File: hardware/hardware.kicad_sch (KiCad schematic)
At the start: 73 parts, among them J1 USB_B, J2 AUDIO, J3 STYLUS, SW1 SW_POWER, U1 NE555P, U2 LM386, U3 LM3914V

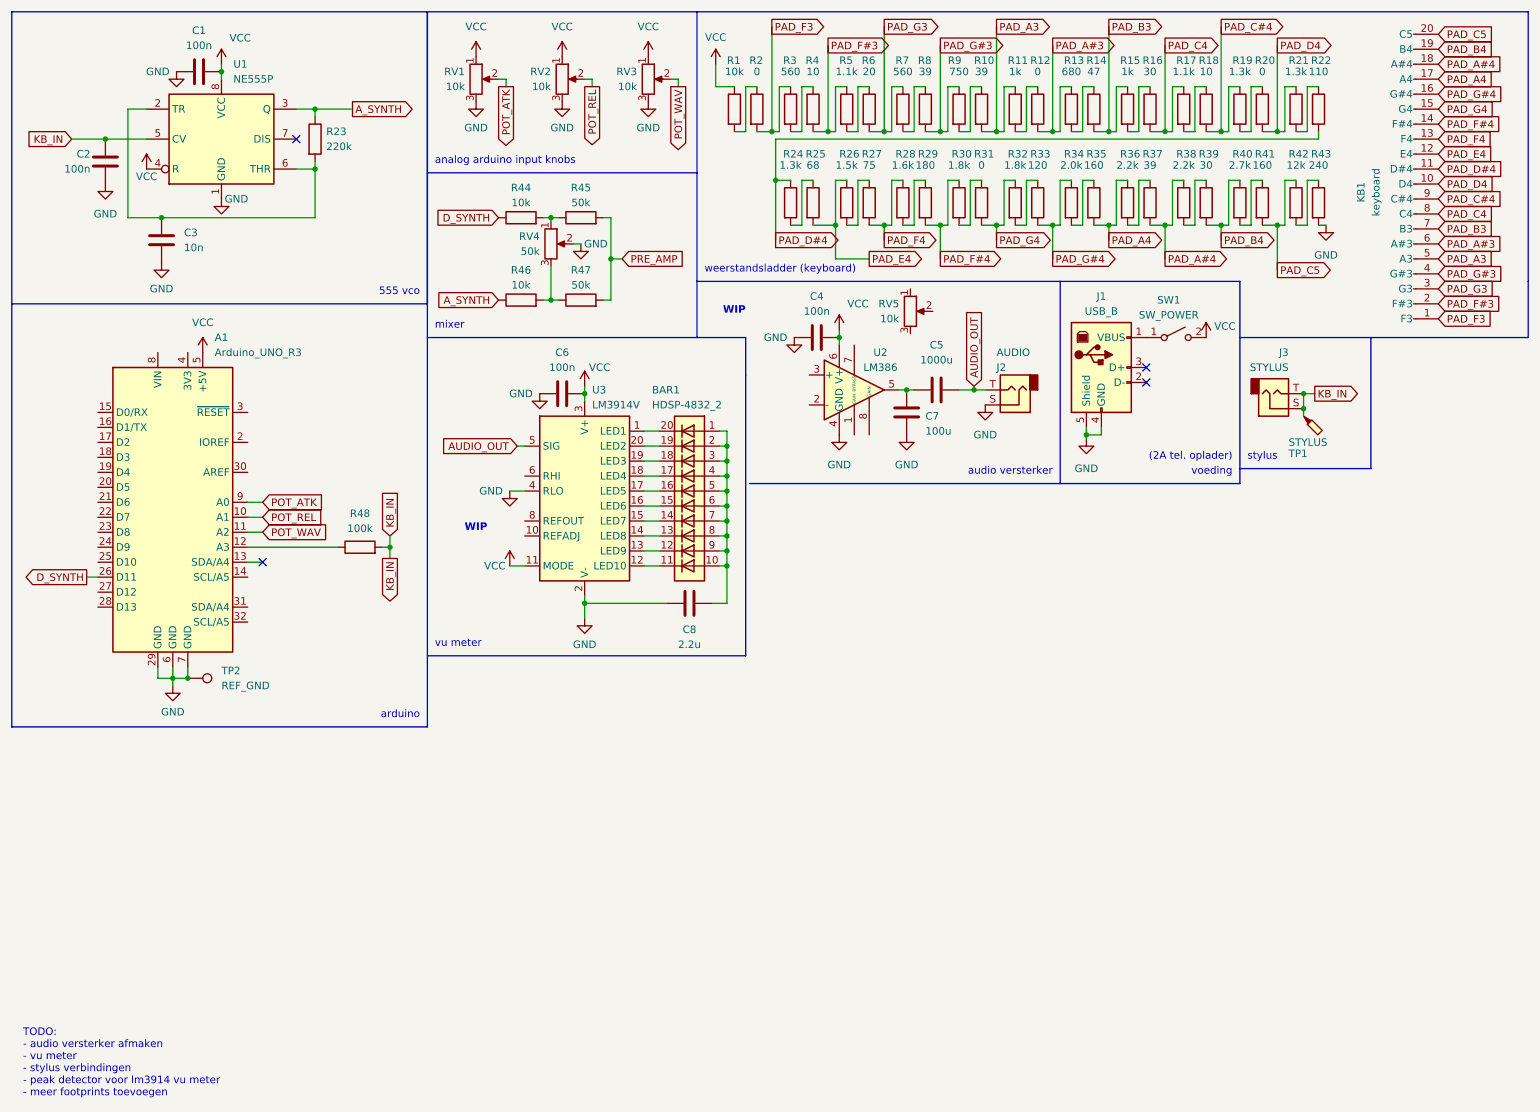
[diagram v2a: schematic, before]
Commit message: more hardware
amplifier circuit done
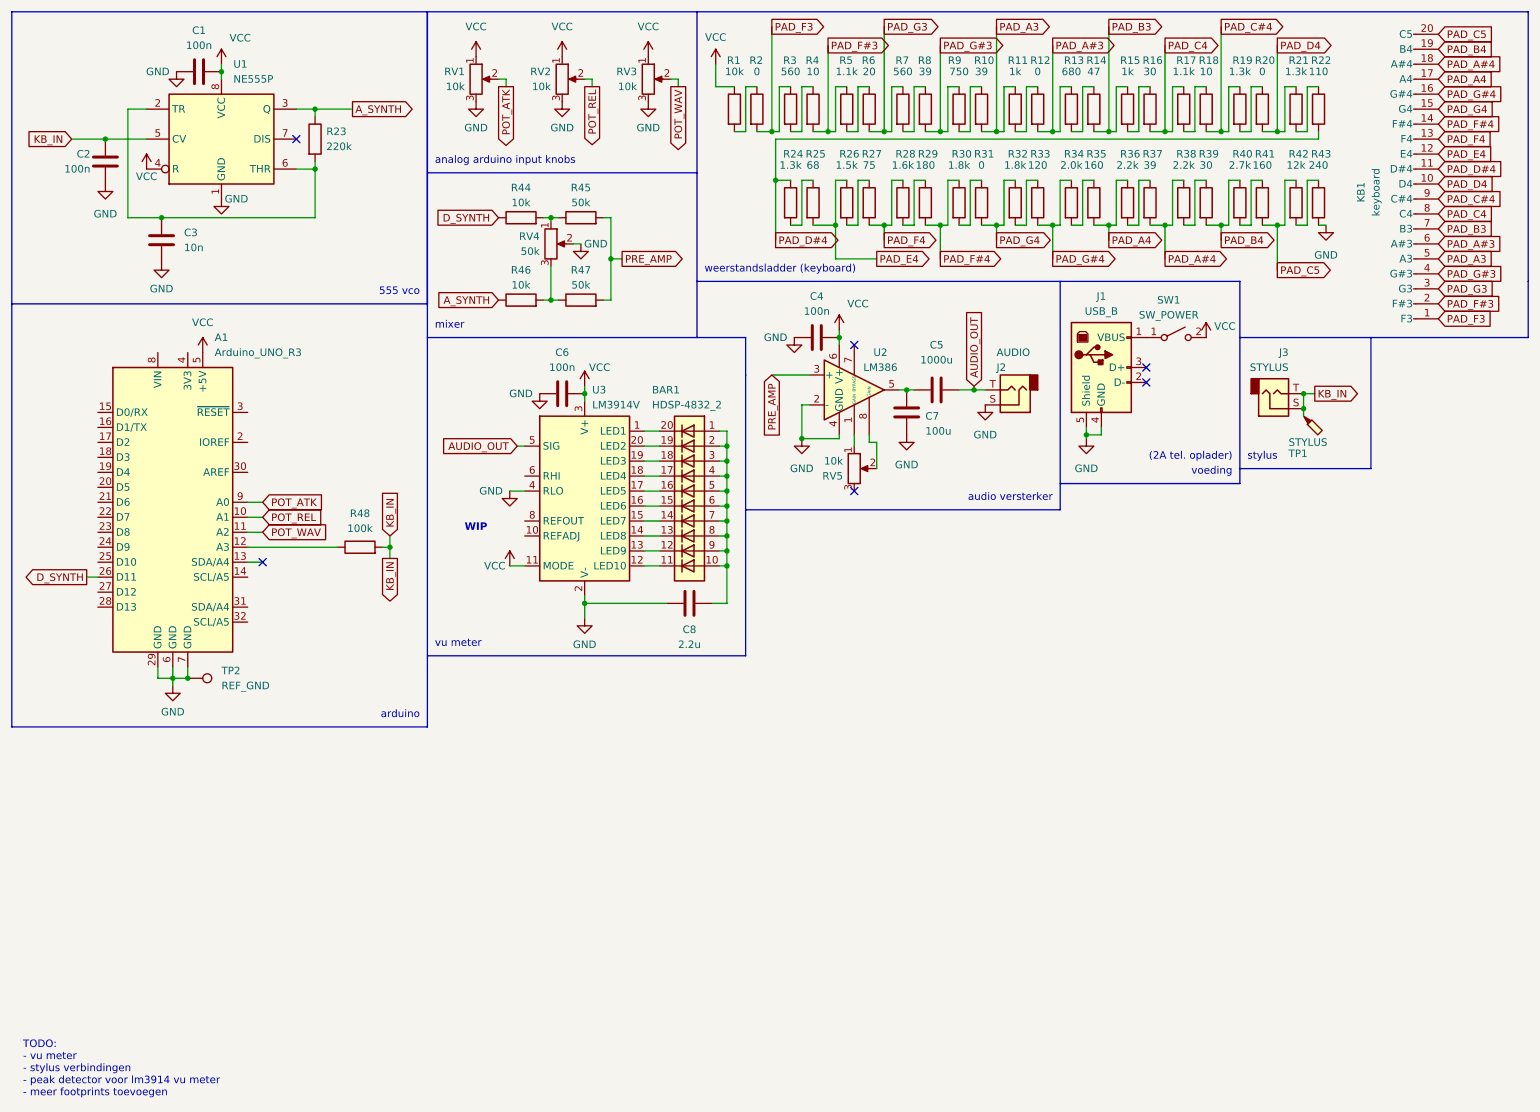
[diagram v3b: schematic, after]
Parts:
- U2: footprint (none) -> Package_DIP:DIP-8_W7.62mm
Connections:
- net GND: now also U2.2 (-)
- net PRE_AMP: now also U2.3 (+)
- net at RV5.1: now also U2.1 (GAIN)
- net at RV5.2: now also U2.8 (GAIN)
- no-connect marks 4 -> 6
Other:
- note added: "TODO: - vu meter - stylus verbindingen - peak detector voor lm3914 vu meter - meer footprints toevoegen"
- note removed: "TODO: - audio versterker afmaken - vu meter - stylus verbindingen - peak detector voor lm3914 vu meter - meer footprints toevoegen"
- moved on the sheet: RV5
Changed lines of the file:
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@@
   (junction (at 198.12 48.26) (diameter 0) (color 0 0 0 0)
   )
+  (junction (at 146.05 84.455) (diameter 0) (color 0 0 0 0)
+  )
   (junction (at 179.07 48.26) (diameter 0) (color 0 0 0 0)
   )
+  (no_connect (at 154.94 68.58))
   (no_connect (at 204.47 74.93))
+  (no_connect (at 154.94 93.345))
   (no_connect (at 54.61 105.41))
   (no_connect (at 204.47 72.39))
@@
     (stroke (width 0) (type default) (color 0 0 0 0))
   )
-  (wire (pts (xy 151.765 53.975) (xy 157.48 53.975))
-    (stroke (width 0) (type default) (color 0 0 0 0))
-  )
   (polyline (pts (xy 128.27 12.065) (xy 128.27 39.37))
     (stroke (width 0) (type default) (color 0 0 0 0))
@@
     (stroke (width 0) (type default) (color 0 0 0 0))
   )
-  (polyline (pts (xy 137.16 92.075) (xy 189.865 92.075))
+  (polyline (pts (xy 136.525 96.52) (xy 189.865 96.52))
     (stroke (width 0) (type default) (color 0 0 0 0))
   )
@@
     (stroke (width 0) (type default) (color 0 0 0 0))
   )
-  (polyline (pts (xy 189.865 92.075) (xy 189.865 57.785))
+  (polyline (pts (xy 189.865 96.52) (xy 189.865 57.785))
     (stroke (width 0) (type default) (color 0 0 0 0))
   )
@@
     (stroke (width 0) (type default) (color 0 0 0 0))
   )
+  (polyline (pts (xy 189.865 92.075) (xy 220.345 92.075))
+    (stroke (width 0) (type default) (color 0 0 0 0))
+  )
   (wire (pts (xy 217.17 48.26) (xy 217.17 50.8))
     (stroke (width 0) (type default) (color 0 0 0 0))
@@
     (stroke (width 0) (type default) (color 0 0 0 0))
   )
+  (wire (pts (xy 147.32 78.74) (xy 146.05 78.74))
+    (stroke (width 0) (type default) (color 0 0 0 0))
+  )
   (wire (pts (xy 133.35 83.185) (xy 132.08 83.185))
     (stroke (width 0) (type default) (color 0 0 0 0))
@@
     (stroke (width 0) (type default) (color 0 0 0 0))
   )
+  (wire (pts (xy 146.05 78.74) (xy 146.05 84.455))
+    (stroke (width 0) (type default) (color 0 0 0 0))
+  )
   (wire (pts (xy 121.92 100.965) (xy 119.38 100.965))
     (stroke (width 0) (type default) (color 0 0 0 0))
@@
     (stroke (width 0) (type default) (color 0 0 0 0))
   )
+  (wire (pts (xy 140.97 73.66) (xy 147.32 73.66))
+    (stroke (width 0) (type default) (color 0 0 0 0))
+  )
   (wire (pts (xy 167.005 48.26) (xy 169.545 48.26))
     (stroke (width 0) (type default) (color 0 0 0 0))
@@
     (stroke (width 0) (type default) (color 0 0 0 0))
   )
+  (wire (pts (xy 158.75 89.535) (xy 158.75 85.09))
+    (stroke (width 0) (type default) (color 0 0 0 0))
+  )
+  (wire (pts (xy 154.94 85.725) (xy 154.94 83.82))
+    (stroke (width 0) (type default) (color 0 0 0 0))
+  )
   (polyline (pts (xy 82.55 67.31) (xy 128.27 67.31))
     (stroke (width 0) (type default) (color 0 0 0 0))
@@
     (stroke (width 0) (type default) (color 0 0 0 0))
   )
+  (wire (pts (xy 151.765 53.975) (xy 158.75 53.975))
+    (stroke (width 0) (type default) (color 0 0 0 0))
+  )
   (wire (pts (xy 151.765 32.385) (xy 150.495 32.385))
     (stroke (width 0) (type default) (color 0 0 0 0))
@@
     (stroke (width 0) (type default) (color 0 0 0 0))
   )
+  (wire (pts (xy 146.05 84.455) (xy 152.4 84.455))
+    (stroke (width 0) (type default) (color 0 0 0 0))
+  )
+  (wire (pts (xy 158.75 85.09) (xy 157.48 85.09))
+    (stroke (width 0) (type default) (color 0 0 0 0))
+  )
   (wire (pts (xy 52.07 105.41) (xy 54.61 105.41))
     (stroke (width 0) (type default) (color 0 0 0 0))
@@
     (stroke (width 0) (type default) (color 0 0 0 0))
   )
-  (polyline (pts (xy 189.865 92.075) (xy 220.345 92.075))
+  (wire (pts (xy 152.4 84.455) (xy 152.4 83.82))
     (stroke (width 0) (type default) (color 0 0 0 0))
   )
@@
     (stroke (width 0) (type default) (color 0 0 0 0))
   )
+  (wire (pts (xy 157.48 85.09) (xy 157.48 83.82))
+    (stroke (width 0) (type default) (color 0 0 0 0))
+  )
   (wire (pts (xy 169.545 48.26) (xy 169.545 53.975))
     (stroke (width 0) (type default) (color 0 0 0 0))
@@
     (effects (font (size 1.27 1.27)) (justify left bottom))
   )
-  (text "TODO:\n- audio versterker afmaken\n- vu meter\n- stylus verbindingen\n- peak detector voor lm3914 vu meter\n- meer footprints toevoegen"
+  (text "TODO:\n- vu meter\n- stylus verbindingen\n- peak detector voor lm3914 vu meter\n- meer footprints toevoegen"
     (at 13.97 196.215 0)
     (effects (font (size 1.27 1.27)) (justify left bottom))
@@
     (effects (font (size 1.27 1.27)) (justify left bottom))
   )
-  (text "audio versterker" (at 188.595 90.805 180)
+  (text "audio versterker" (at 188.595 95.25 180)
     (effects (font (size 1.27 1.27)) (justify right bottom))
   )
@@
     (effects (font (size 1.27 1.27)) (justify right bottom))
   )
-  (text "WIP" (at 136.525 63.5 180)
-    (effects (font (size 1.27 1.27) (thickness 0.254) bold) (justify right bottom))
-  )
   (text "mixer\n" (at 83.82 66.04 0)
     (effects (font (size 1.27 1.27)) (justify left bottom))
@@
     )
   )
+  (global_label "PRE_AMP" (shape input) (at 140.97 73.66 270) (fields_autoplaced)
+    (effects (font (size 1.27 1.27)) (justify right))
+    (property "Intersheet References" "${INTERSHEET_REFS}" (id 0) (at 141.0494 84.5398 90)
+      (effects (font (size 1.27 1.27)) (justify right) hide)
+    )
+  )
   (global_label "PAD_B4" (shape output) (at 217.17 50.8 0) (fields_autoplaced)
     (effects (font (size 1.27 1.27)) (justify left))
@@
     )
   )
-  (global_label "PRE_AMP" (shape input) (at 115.57 53.975 0) (fields_autoplaced)
+  (global_label "PRE_AMP" (shape output) (at 115.57 53.975 0) (fields_autoplaced)
     (effects (font (size 1.27 1.27)) (justify left))
     (property "Intersheet References" "${INTERSHEET_REFS}" (id 0) (at 126.4498 53.8956 0)
@@
     )
   )
-  (global_label "PAD_E4" (shape output) (at 157.48 53.975 0) (fields_autoplaced)
+  (global_label "PAD_E4" (shape output) (at 158.75 53.975 0) (fields_autoplaced)
     (effects (font (size 1.27 1.27)) (justify left))
-    (property "Intersheet References" "${INTERSHEET_REFS}" (id 0) (at 166.8479 53.8956 0)
+    (property "Intersheet References" "${INTERSHEET_REFS}" (id 0) (at 168.1179 53.8956 0)
       (effects (font (size 1.27 1.27)) (justify left) hide)
     )
@@
     (pin "2")
   )
-  (symbol (lib_id "power:GND") (at 109.22 114.935 0) (unit 1)
+  (symbol (lib_id "power:GND") (at 146.05 84.455 0) (unit 1)
     (in_bom yes) (on_board yes) (fields_autoplaced)
-    (property "Reference" "#PWR028" (id 0) (at 109.22 121.285 0)
+    (property "Reference" "#PWR?" (id 0) (at 146.05 90.805 0)
       (effects (font (size 1.27 1.27)) hide)
     )
-    (property "Value" "GND" (id 1) (at 109.22 119.38 0))
-    (property "Footprint" "" (id 2) (at 109.22 114.935 0)
+    (property "Value" "GND" (id 1) (at 146.05 89.535 0))
+    (property "Footprint" "" (id 2) (at 146.05 84.455 0)
       (effects (font (size 1.27 1.27)) hide)
     )
-    (property "Datasheet" "" (id 3) (at 109.22 114.935 0)
+    (property "Datasheet" "" (id 3) (at 146.05 84.455 0)
       (effects (font (size 1.27 1.27)) hide)
     )
     (pin "1")
   )
-  (symbol (lib_id "power:GND") (at 152.4 83.82 0) (unit 1)
+  (symbol (lib_id "power:GND") (at 109.22 114.935 0) (unit 1)
     (in_bom yes) (on_board yes) (fields_autoplaced)
-    (property "Reference" "#PWR023" (id 0) (at 152.4 90.17 0)
+    (property "Reference" "#PWR028" (id 0) (at 109.22 121.285 0)
       (effects (font (size 1.27 1.27)) hide)
     )
-    (property "Value" "GND" (id 1) (at 152.4 88.9 0))
-    (property "Footprint" "" (id 2) (at 152.4 83.82 0)
+    (property "Value" "GND" (id 1) (at 109.22 119.38 0))
+    (property "Footprint" "" (id 2) (at 109.22 114.935 0)
       (effects (font (size 1.27 1.27)) hide)
     )
-    (property "Datasheet" "" (id 3) (at 152.4 83.82 0)
+    (property "Datasheet" "" (id 3) (at 109.22 114.935 0)
       (effects (font (size 1.27 1.27)) hide)
     )
@@
     (pin "T")
   )
-  (symbol (lib_id "Device:R_Potentiometer") (at 164.465 62.865 0) (unit 1)
+  (symbol (lib_id "Device:R_Potentiometer") (at 154.94 89.535 0) (unit 1)
     (in_bom yes) (on_board yes)
-    (property "Reference" "RV5" (id 0) (at 162.56 61.595 0)
+    (property "Reference" "RV5" (id 0) (at 153.035 90.805 0)
       (effects (font (size 1.27 1.27)) (justify right))
     )
-    (property "Value" "10k" (id 1) (at 162.56 64.135 0)
+    (property "Value" "10k" (id 1) (at 153.035 88.265 0)
       (effects (font (size 1.27 1.27)) (justify right))
     )
-    (property "Footprint" "keyboard:potm" (id 2) (at 164.465 62.865 0)
+    (property "Footprint" "keyboard:potm" (id 2) (at 154.94 89.535 0)
       (effects (font (size 1.27 1.27)) hide)
     )
-    (property "Datasheet" "~" (id 3) (at 164.465 62.865 0)
+    (property "Datasheet" "~" (id 3) (at 154.94 89.535 0)
       (effects (font (size 1.27 1.27)) hide)
     )
@@
     (property "Reference" "U2" (id 0) (at 159.385 69.85 0))
     (property "Value" "LM386" (id 1) (at 159.385 72.39 0))
-    (property "Footprint" "" (id 2) (at 157.48 73.66 0)
+    (property "Footprint" "Package_DIP:DIP-8_W7.62mm" (id 2) (at 157.48 73.66 0)
       (effects (font (size 1.27 1.27)) hide)
     )
@@
       (reference "#PWR022") (unit 1) (value "GND") (footprint "")
     )
-    (path "/0f53a7cb-a1ba-402c-b627-13d9057eb127"
-      (reference "#PWR023") (unit 1) (value "GND") (footprint "")
-    )
     (path "/c0a4e59a-2242-4ff3-a3b6-e1b8f7277d35"
       (reference "#PWR024") (unit 1) (value "GND") (footprint "")
@@
       (reference "#PWR029") (unit 1) (value "GND") (footprint "")
     )
+    (path "/07d6f954-f048-445f-a3c0-332affd131c7"
+      (reference "#PWR?") (unit 1) (value "GND") (footprint "")
+    )
     (path "/2102c637-9f11-48f1-aae6-b4139dc22be2"
       (reference "A1") (unit 1) (value "Arduino_UNO_R3") (footprint "Module:Arduino_UNO_R3")
@@
     )
     (path "/8634edb8-50db-43d2-95bb-5918d2cd24cc"
-      (reference "U2") (unit 1) (value "LM386") (footprint "")
+      (reference "U2") (unit 1) (value "LM386") (footprint "Package_DIP:DIP-8_W7.62mm")
     )
     (path "/6861c69a-2093-46f7-addc-65485166ba0a"

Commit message: more hardware (almost done!)
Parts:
- removed TP2: REF_GND, symbol Connector:TestPoint
- added C11: 10n, symbol Device:C
- added C6: C, symbol Device:C
- added C9: 10u, symbol Device:C
- added D1: D, symbol Device:D
- added R48: 100k, symbol Device:R
- added R49: 1k, symbol Device:R
- renumbered C8 to C10, C6 to C4, C4 to C5, C5 to C7, C7 to C8, R48 to R50, U3 to U2, U2 to U3
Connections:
- net AUDIO_OUT: now also D1.2 (A); no longer U2.5 (SIG)
- net D_SYNTH: now also C9.1; no longer A1.26 (D11)
- net GND: now also C11.2, C6.2, R48.2
- net at RV5.1: no longer U3.1 (GAIN)
- net at RV5.2: now also U3.1 (GAIN); no longer U3.8 (GAIN)
- net at RV5.3: now also U3.8 (GAIN)
- new net: C11.1, C9.2, R49.1
- new net: A1.26 (D11), R49.2
- new net: C6.1, D1.1 (K), R48.1, U2.5 (SIG)
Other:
- note added: "TODO: - meer footprints toevoegen"
- note removed: "TODO: - vu meter - stylus verbindingen - peak detector voor lm3914 vu meter - meer footprints toevoegen"
- note removed: "WIP"
- moved on the sheet: A1, BAR1, C10, C4, C5, C7, C8, J1, J2, J3, R50, RV5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

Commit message: more hardware
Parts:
- added RV6: DISP_SENS, symbol Device:R_Potentiometer
- BAR1: value HDSP-4832_2 -> HDSP-4832
- C6: value C -> 1u
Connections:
- net GND: now also RV6.3
- net VCC: now also BAR1.1 (A), BAR1.10 (A), BAR1.2 (A), BAR1.3 (A), BAR1.4 (A), BAR1.5 (A), BAR1.6 (A), BAR1.7 (A), BAR1.8 (A), BAR1.9 (A), C10.1
- net at U2.1 (LED1): now also BAR1.11 (K); no longer BAR1.20 (K)
- net at U2.10 (REFADJ): now also RV6.2
- net at U2.12 (LED10): now also BAR1.20 (K); no longer BAR1.11 (K)
- net at U2.13 (LED9): now also BAR1.19 (K); no longer BAR1.12 (K)
- net at U2.14 (LED8): now also BAR1.18 (K); no longer BAR1.13 (K)
- net at U2.15 (LED7): now also BAR1.17 (K); no longer BAR1.14 (K)
- net at U2.16 (LED6): now also BAR1.16 (K); no longer BAR1.15 (K)
- net at U2.17 (LED5): now also BAR1.15 (K); no longer BAR1.16 (K)
- net at U2.18 (LED4): now also BAR1.14 (K); no longer BAR1.17 (K)
- net at U2.19 (LED3): now also BAR1.13 (K); no longer BAR1.18 (K)
- net at U2.20 (LED2): now also BAR1.12 (K); no longer BAR1.19 (K)
- net at U2.6 (RHI): now also U2.8 (REFOUT), RV6.1
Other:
- moved on the sheet: BAR1

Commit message: more hardware
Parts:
- added C12: 100n, Capacitor_THT:C_Disc_D3.0mm_W1.6mm_P2.50mm, symbol Device:C
- C1, C11, C2, C3, C4, C5: footprint (none) -> Capacitor_THT:C_Disc_D3.0mm_W1.6mm_P2.50mm
- C10, C6: footprint (none) -> Capacitor_THT:CP_Radial_D5.0mm_P2.00mm
- C7: value 1000u -> 1u; footprint (none) -> Capacitor_THT:CP_Radial_D5.0mm_P2.00mm
- C8, C9: footprint (none) -> Capacitor_THT:CP_Radial_D10.0mm_P2.50mm
- D1: footprint (none) -> Diode_THT:D_A-405_P7.62mm_Horizontal
- R48, R49: footprint (none) -> Resistor_THT:R_Axial_DIN0207_L6.3mm_D2.5mm_P10.16mm_Horizontal
- RV6: value DISP_SENS -> 4k7; footprint (none) -> Potentiometer_THT:Potentiometer_Piher_PT-10-V10_Vertical
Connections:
- net GND: now also C12.1
- net VCC: now also C12.2
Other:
- moved on the sheet: RV6

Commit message: hardware done
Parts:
- added J1: PJ_AKI, Connector_PinHeader_2.54mm:PinHeader_1x02_P2.54mm_Vertical, symbol Connector_Generic:Conn_02x01
- added J2: PJ_AAO, Connector_PinHeader_2.54mm:PinHeader_1x02_P2.54mm_Vertical, symbol Connector_Generic:Conn_02x01
- added J5: PJ_PAO, Connector_PinHeader_2.54mm:PinHeader_1x02_P2.54mm_Vertical, symbol Connector_Generic:Conn_02x01
- added J7: PJ_DAI, Connector_PinHeader_2.54mm:PinHeader_1x02_P2.54mm_Vertical, symbol Connector_Generic:Conn_02x01
- added J8: PJ_MAO, Connector_PinHeader_2.54mm:PinHeader_1x02_P2.54mm_Vertical, symbol Connector_Generic:Conn_02x01
- added J9: PJ_AAI, Connector_PinHeader_2.54mm:PinHeader_1x02_P2.54mm_Vertical, symbol Connector_Generic:Conn_02x01
- SW1: footprint (none) -> Button_Switch_THT:SW_Slide_1P2T_CK_OS102011MS2Q
- renumbered C9 to C10, C10 to C11, C11 to C12, C12 to C5, C5 to C6, C6 to C7, C7 to C8, C8 to C9, J1 to J3, J3 to J4, J2 to J6, R48 to R44, R49 to R45, R50 to R46, R44 to R47, R45 to R48, R46 to R49, R47 to R50, RV6 to RV4, RV4 to RV6
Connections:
- net AUDIO_OUT: now also J5.2 (Pin_2); no longer C8.2, J6.T
- net A_SYNTH: now also J2.2 (Pin_2), J9.1 (Pin_1); no longer R23.1, R49.1, U1.3 (Q)
- net D_SYNTH: now also J7.1 (Pin_1); no longer R47.1
- net KB_IN: now also J1.1 (Pin_1); no longer C2.1, U1.5 (CV)
- net PRE_AMP: now also J8.2 (Pin_2); no longer R48.2, R50.2
- new net: C8.2, J5.1 (Pin_1), J6.T
- new net: J8.1 (Pin_1), R48.2, R50.2
- new net: J7.2 (Pin_2), R47.1
- new net: C2.1, J1.2 (Pin_2), U1.5 (CV)
- new net: J2.1 (Pin_1), R23.1, U1.3 (Q)
- new net: J9.2 (Pin_2), R49.1
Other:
- moved on the sheet: J3, J4, R47, R48, R49, R50, RV6, SW1, TP1

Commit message: hardware gesoldeerd
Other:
- note removed: "TODO: - meer footprints toevoegen"
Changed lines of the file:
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@@
-    (effects (font (size 1.27 1.27)) (justify left bottom))
-  )
-  (text "TODO:\n- meer footprints toevoegen" (at 13.97 196.215 0)
     (effects (font (size 1.27 1.27)) (justify left bottom))
   )
